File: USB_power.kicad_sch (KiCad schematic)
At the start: 30 parts, among them J16 USB_C_Receptacle_PowerOnly_6P, Q3 DMP3013SFV, Q4 DMP3013SFV, U5 CYPD3177-24LQ

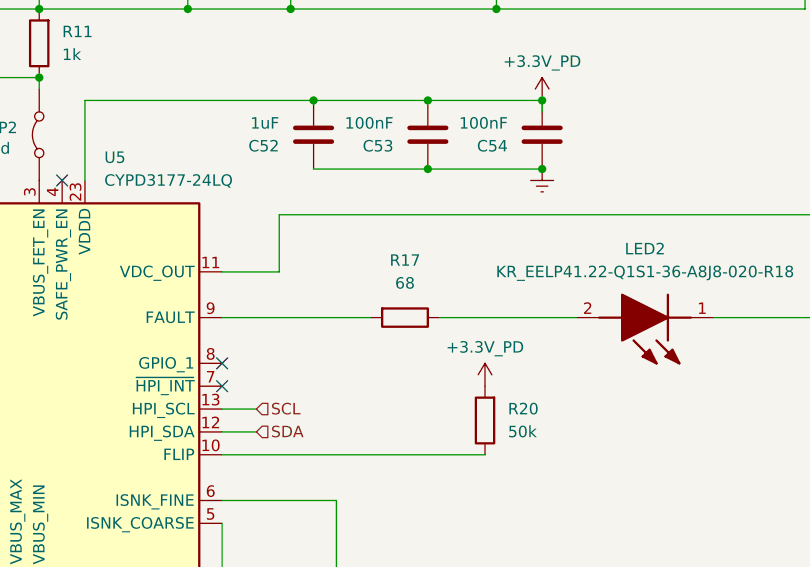
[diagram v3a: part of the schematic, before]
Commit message: 1k led resistors. top silkscreen
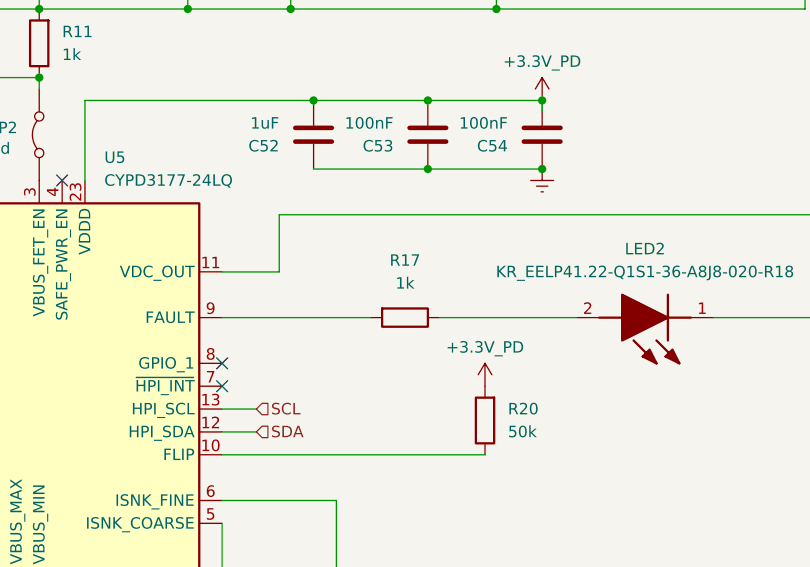
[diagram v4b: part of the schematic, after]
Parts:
- R17: value 68 -> 1k
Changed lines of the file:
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@@
 			)
 		)
-		(property "Value" "68"
+		(property "Value" "1k"
 			(at 160.02 99.06 90)
 			(effects
